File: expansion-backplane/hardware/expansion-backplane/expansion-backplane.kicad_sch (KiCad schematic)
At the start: 15 parts, among them J1 Barrel_Jack, SW1 SW_SPST

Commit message: added expansion connector
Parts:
- D1: footprint (none) -> LED_THT:LED_D3.0mm
- R1: footprint (none) -> Resistor_THT:R_Axial_DIN0207_L6.3mm_D2.5mm_P7.62mm_Horizontal
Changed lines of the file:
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@@
 			)
 		)
-		(property "Footprint" ""
+		(property "Footprint" "LED_THT:LED_D3.0mm"
 			(at 71.12 34.29 0)
 			(effects
@@
 			)
 		)
-		(property "Footprint" ""
+		(property "Footprint" "Resistor_THT:R_Axial_DIN0207_L6.3mm_D2.5mm_P7.62mm_Horizontal"
 			(at 69.342 44.45 90)
 			(effects

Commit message: wip
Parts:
- removed SW1: SW_SPST, symbol Switch:SW_SPST
- added SW1: SW_SPDT, minimal-64x4:E-Switch_200MSP1T2B2M6RE, symbol Switch:SW_SPDT
- C1: renamed from C2; footprint (none) -> Capacitor_THT:CP_Radial_D4.0mm_P2.00mm
- C2: renamed from C1; footprint (none) -> Capacitor_THT:CP_Radial_D5.0mm_P2.00mm
- C3, C4, C5, C6: footprint (none) -> Capacitor_THT:CP_Radial_D4.0mm_P2.00mm
- CN1, CN2, CN3, CN4, CN5: footprint Connector_PinSocket_2.54mm:PinSocket_2x32_P2.54mm_Vertical -> Connector_PinSocket_2.54mm:PinSocket_2x16_P2.54mm_Vertical
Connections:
- net +5V: now also SW1.1 (A)
- net at J1.1: now also SW1.2 (B)
- no-connect marks 0 -> 1
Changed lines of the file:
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@@
 	)
 	(junction
-		(at 71.12 30.48)
+		(at 170.18 95.25)
 		(diameter 0)
 		(color 0 0 0 0)
 	)
 	(junction
-		(at 170.18 95.25)
+		(at 215.9 95.25)
 		(diameter 0)
 		(color 0 0 0 0)
 	)
 	(junction
-		(at 215.9 95.25)
+		(at 71.12 30.48)
 		(diameter 0)
 		(color 0 0 0 0)
 	)
+	(no_connect
+		(at 67.31 33.02)
+	)
 	(wire
 		(pts
@@
 	(wire
 		(pts
+			(xy 71.12 27.94) (xy 71.12 30.48)
+		)
+		(stroke
+			(width 0)
+			(type default)
+		)
+	)
+	(wire
+		(pts
 			(xy 81.28 48.26) (xy 81.28 38.1)
 		)
@@
 	(wire
 		(pts
+			(xy 67.31 27.94) (xy 71.12 27.94)
+		)
+		(stroke
+			(width 0)
+			(type default)
+		)
+	)
+	(wire
+		(pts
 			(xy 38.1 95.25) (xy 40.64 95.25)
 		)
@@
 	(wire
 		(pts
-			(xy 67.31 30.48) (xy 71.12 30.48)
-		)
-		(stroke
-			(width 0)
-			(type default)
-		)
-	)
-	(wire
-		(pts
 			(xy 83.82 95.25) (xy 83.82 85.09)
 		)
@@
 		(on_board yes)
 		(dnp no)
-		(property "Reference" "C2"
+		(property "Reference" "C1"
 			(at 50.8 79.248 90)
 			(effects
@@
 			)
 		)
-		(property "Footprint" ""
+		(property "Footprint" "Capacitor_THT:CP_Radial_D4.0mm_P2.00mm"
 			(at 54.61 84.1248 0)
 			(effects
@@
 			(project "expansion-backplane"
 				(path "/e49372f6-369a-421a-b977-37c09b53354c"
-					(reference "C2")
+					(reference "C1")
 					(unit 1)
 				)
@@
 		(dnp no)
 		(fields_autoplaced yes)
-		(property "Reference" "#PWR02"
+		(property "Reference" "#PWR01"
 			(at 38.1 99.06 0)
 			(effects
@@
 			(project "expansion-backplane"
 				(path "/e49372f6-369a-421a-b977-37c09b53354c"
-					(reference "#PWR02")
+					(reference "#PWR01")
 					(unit 1)
 				)
@@
 			)
 		)
-		(property "Footprint" "Connector_PinSocket_2.54mm:PinSocket_2x32_P2.54mm_Vertical"
+		(property "Footprint" "Connector_PinSocket_2.54mm:PinSocket_2x16_P2.54mm_Vertical"
 			(at 129.794 34.29 0)
 			(effects
@@
 		(dnp no)
 		(fields_autoplaced yes)
-		(property "Reference" "#PWR010"
+		(property "Reference" "#PWR012"
 			(at 238.76 88.9 0)
 			(effects
@@
 			(project "expansion-backplane"
 				(path "/e49372f6-369a-421a-b977-37c09b53354c"
-					(reference "#PWR010")
+					(reference "#PWR012")
 					(unit 1)
 				)
@@
 		(dnp no)
 		(fields_autoplaced yes)
-		(property "Reference" "C1"
+		(property "Reference" "C2"
 			(at 84.201 32.1888 0)
 			(effects
@@
 			)
 		)
-		(property "Footprint" ""
+		(property "Footprint" "Capacitor_THT:CP_Radial_D5.0mm_P2.00mm"
 			(at 82.2452 38.1 0)
 			(effects
@@
 			(project "expansion-backplane"
 				(path "/e49372f6-369a-421a-b977-37c09b53354c"
-					(reference "C1")
+					(reference "C2")
 					(unit 1)
 				)
@@
 		(dnp no)
 		(fields_autoplaced yes)
-		(property "Reference" "#PWR09"
+		(property "Reference" "#PWR011"
 			(at 213.36 99.06 0)
 			(effects
@@
 			(project "expansion-backplane"
 				(path "/e49372f6-369a-421a-b977-37c09b53354c"
-					(reference "#PWR09")
+					(reference "#PWR011")
 					(unit 1)
 				)
@@
 	)
 	(symbol
+		(lib_id "Switch:SW_SPDT")
+		(at 62.23 30.48 0)
+		(unit 1)
+		(exclude_from_sim no)
+		(in_bom yes)
+		(on_board yes)
+		(dnp no)
+		(fields_autoplaced yes)
+		(property "Reference" "SW1"
+			(at 62.23 22.6525 0)
+			(effects
+				(font
+					(size 1.27 1.27)
+				)
+			)
+		)
+		(property "Value" "SW_SPDT"
+			(at 62.23 25.0768 0)
+			(effects
+				(font
+					(size 1.27 1.27)
+				)
+			)
+		)
+		(property "Footprint" "minimal-64x4:E-Switch_200MSP1T2B2M6RE"
+			(at 62.23 30.48 0)
+			(effects
+				(font
+					(size 1.27 1.27)
+				)
+				(hide yes)
+			)
+		)
+		(property "Datasheet" "https://configured-product-images.s3.amazonaws.com/2D/specs/200MSP1T2B2M6RE.pdf"
+			(at 62.23 38.1 0)
+			(effects
+				(font
+					(size 1.27 1.27)
+				)
+				(hide yes)
+			)
+		)
+		(property "Description" "Switch, single pole double throw"
+			(at 62.23 30.48 0)
+			(effects
+				(font
+					(size 1.27 1.27)
+				)
+				(hide yes)
+			)
+		)
+		(pin "2"
+		)
+		(pin "1"
+		)
+		(pin "3"
+		)
+		(instances
+			(project "expansion-backplane"
+				(path "/e49372f6-369a-421a-b977-37c09b53354c"
+					(reference "SW1")
+					(unit 1)
+				)
+			)
+		)
+	)
+	(symbol
 		(lib_name "min-64x4-expansion_1")
 		(lib_id "minimal-64x4:min-64x4-expansion")
@@
 			)
 		)
-		(property "Footprint" "Connector_PinSocket_2.54mm:PinSocket_2x32_P2.54mm_Vertical"
+		(property "Footprint" "Connector_PinSocket_2.54mm:PinSocket_2x16_P2.54mm_Vertical"
 			(at 261.874 34.29 0)
 			(effects
@@
 			)
 		)
-		(property "Footprint" ""
+		(property "Footprint" "Capacitor_THT:CP_Radial_D4.0mm_P2.00mm"
 			(at 184.15 84.1248 0)
 			(effects
@@
 		(dnp no)
 		(fields_autoplaced yes)
-		(property "Reference" "#PWR05"
+		(property "Reference" "#PWR07"
 			(at 124.46 99.06 0)
 			(effects
@@
 			(project "expansion-backplane"
 				(path "/e49372f6-369a-421a-b977-37c09b53354c"
-					(reference "#PWR05")
+					(reference "#PWR07")
 					(unit 1)
 				)
@@
 		(dnp no)
 		(fields_autoplaced yes)
-		(property "Reference" "#PWR011"
+		(property "Reference" "#PWR05"
 			(at 90.17 54.61 0)
 			(effects
@@
 			(project "expansion-backplane"
 				(path "/e49372f6-369a-421a-b977-37c09b53354c"
-					(reference "#PWR011")
+					(reference "#PWR05")
 					(unit 1)
 				)
@@
 			)
 		)
-		(property "Footprint" "Connector_PinSocket_2.54mm:PinSocket_2x32_P2.54mm_Vertical"
+		(property "Footprint" "Connector_PinSocket_2.54mm:PinSocket_2x16_P2.54mm_Vertical"
 			(at 86.614 34.29 0)
 			(effects
@@
 			)
 		)
-		(property "Footprint" ""
+		(property "Footprint" "Capacitor_THT:CP_Radial_D4.0mm_P2.00mm"
 			(at 97.79 84.1248 0)
 			(effects
@@
 		(dnp no)
 		(fields_autoplaced yes)
-		(property "Reference" "#PWR07"
+		(property "Reference" "#PWR09"
 			(at 167.64 99.06 0)
 			(effects
@@
 			(project "expansion-backplane"
 				(path "/e49372f6-369a-421a-b977-37c09b53354c"
-					(reference "#PWR07")
+					(reference "#PWR09")
 					(unit 1)
 				)
@@
 			)
 		)
-		(property "Footprint" ""
+		(property "Footprint" "Capacitor_THT:CP_Radial_D4.0mm_P2.00mm"
 			(at 229.87 84.1248 0)
 			(effects
@@
 	)
 	(symbol
-		(lib_id "Switch:SW_SPST")
-		(at 62.23 30.48 0)
-		(unit 1)
-		(exclude_from_sim no)
-		(in_bom yes)
-		(on_board yes)
-		(dnp no)
-		(fields_autoplaced yes)
-		(property "Reference" "SW1"
-			(at 62.23 24.6845 0)
-			(effects
-				(font
-					(size 1.27 1.27)
-				)
-			)
-		)
-		(property "Value" "SW_SPST"
-			(at 62.23 27.1088 0)
-			(effects
-				(font
-					(size 1.27 1.27)
-				)
-			)
-		)
-		(property "Footprint" ""
-			(at 62.23 30.48 0)
-			(effects
-				(font
-					(size 1.27 1.27)
-				)
-				(hide yes)
-			)
-		)
-		(property "Datasheet" "~"
-			(at 62.23 30.48 0)
-			(effects
-				(font
-					(size 1.27 1.27)
-				)
-				(hide yes)
-			)
-		)
-		(property "Description" "Single Pole Single Throw (SPST) switch"
-			(at 62.23 30.48 0)
-			(effects
-				(font
-					(size 1.27 1.27)
-				)
-				(hide yes)
-			)
-		)
-		(pin "1"
-		)
-		(pin "2"
-		)
-		(instances
-			(project "expansion-backplane"
-				(path "/e49372f6-369a-421a-b977-37c09b53354c"
-					(reference "SW1")
-					(unit 1)
-				)
-			)
-		)
-	)
-	(symbol
 		(lib_id "power:GND")
 		(at 63.5 95.25 180)
@@
 		(dnp no)
 		(fields_autoplaced yes)
-		(property "Reference" "#PWR01"
+		(property "Reference" "#PWR02"
 			(at 63.5 88.9 0)
 			(effects
@@
 			(project "expansion-backplane"
 				(path "/e49372f6-369a-421a-b977-37c09b53354c"
-					(reference "#PWR01")
+					(reference "#PWR02")
 					(unit 1)
 				)
@@
 		(dnp no)
 		(fields_autoplaced yes)
-		(property "Reference" "#PWR06"
+		(property "Reference" "#PWR08"
 			(at 149.86 88.9 0)
 			(effects
@@
 			(project "expansion-backplane"
 				(path "/e49372f6-369a-421a-b977-37c09b53354c"
-					(reference "#PWR06")
+					(reference "#PWR08")
 					(unit 1)
 				)
@@
 		(dnp no)
 		(fields_autoplaced yes)
-		(property "Reference" "#PWR08"
+		(property "Reference" "#PWR010"
 			(at 193.04 88.9 0)
 			(effects
@@
 			(project "expansion-backplane"
 				(path "/e49372f6-369a-421a-b977-37c09b53354c"
-					(reference "#PWR08")
+					(reference "#PWR010")
 					(unit 1)
 				)
@@
 		(dnp no)
 		(fields_autoplaced yes)
-		(property "Reference" "#PWR04"
+		(property "Reference" "#PWR06"
 			(at 106.68 88.9 0)
 			(effects
@@
 			(project "expansion-backplane"
 				(path "/e49372f6-369a-421a-b977-37c09b53354c"
-					(reference "#PWR04")
+					(reference "#PWR06")
 					(unit 1)
 				)
@@
 			)
 		)
-		(property "Footprint" "Connector_PinSocket_2.54mm:PinSocket_2x32_P2.54mm_Vertical"
+		(property "Footprint" "Connector_PinSocket_2.54mm:PinSocket_2x16_P2.54mm_Vertical"
 			(at 172.974 34.29 0)
 			(effects
@@
 		(dnp no)
 		(fields_autoplaced yes)
-		(property "Reference" "#PWR012"
+		(property "Reference" "#PWR04"
 			(at 90.17 34.29 0)
 			(effects
@@
 			(project "expansion-backplane"
 				(path "/e49372f6-369a-421a-b977-37c09b53354c"
-					(reference "#PWR012")
+					(reference "#PWR04")
 					(unit 1)
 				)
@@
 			)
 		)
-		(property "Footprint" ""
+		(property "Footprint" "Capacitor_THT:CP_Radial_D4.0mm_P2.00mm"
 			(at 140.97 84.1248 0)
 			(effects
@@
 			)
 		)
-		(property "Footprint" "Connector_PinSocket_2.54mm:PinSocket_2x32_P2.54mm_Vertical"
+		(property "Footprint" "Connector_PinSocket_2.54mm:PinSocket_2x16_P2.54mm_Vertical"
 			(at 216.154 34.29 0)
 			(effects

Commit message: improved backplane
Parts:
- added C4: 0.1 uF, Capacitor_THT:C_Disc_D3.8mm_W2.6mm_P2.50mm, symbol Device:C
- added U1: 74LS126, Package_DIP:DIP-14_W7.62mm, symbol 74xx:74LS126
- renumbered C4 to C5, C5 to C6, C6 to C7
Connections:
- net +5V: now also C4.1, U1.12, U1.14 (VCC), U1.2, U1.5, U1.9
- net GND: now also C4.2, U1.7 (GND)
- net USER: no longer CN5.4 (NC)
- removed net INH: CN1.3 (INH), CN2.3 (INH), CN3.3 (INH), CN4.3 (INH), CN5.3 (INH)
- new net: CN2.3 (INH), U1.4
- new net: CN5.3 (INH), U1.11, U1.3, U1.6, U1.8
- new net: CN4.3 (INH), U1.13
- new net: CN3.3 (INH), U1.10
- new net: CN1.3 (INH), U1.1

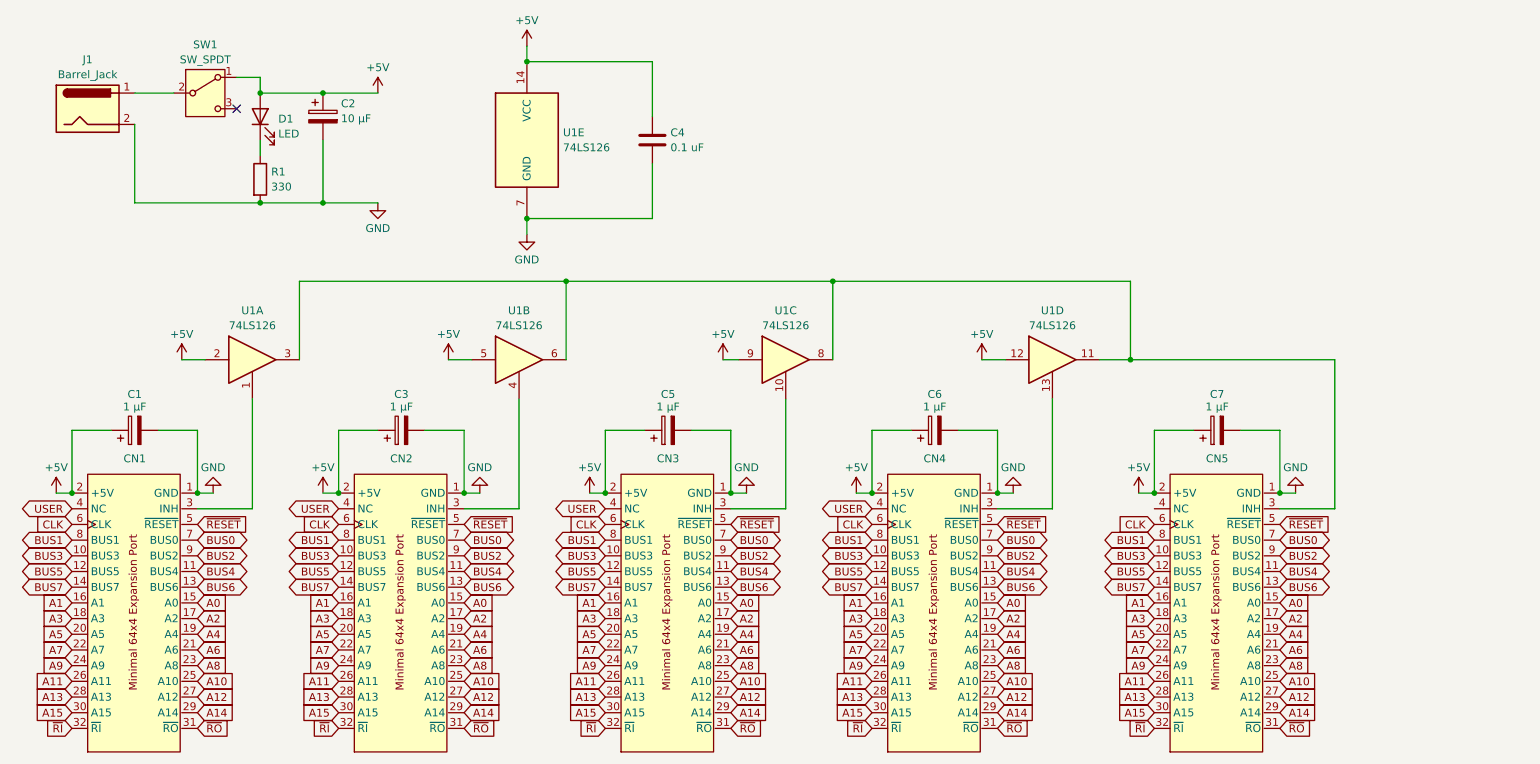
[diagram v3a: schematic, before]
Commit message: added pull down resistors
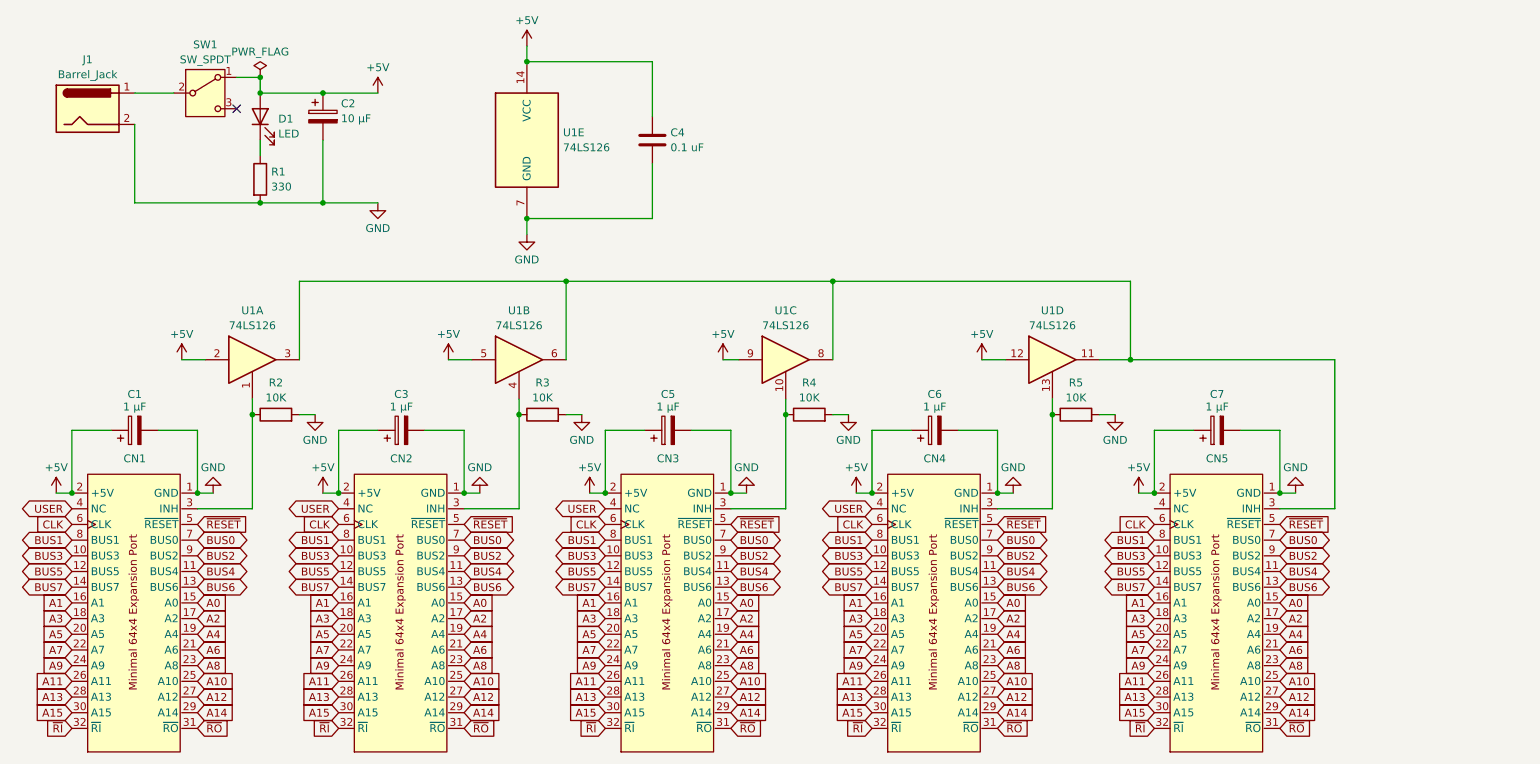
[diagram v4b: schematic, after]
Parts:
- added R2, R3, R4, R5: 10K, Resistor_THT:R_Axial_DIN0207_L6.3mm_D2.5mm_P7.62mm_Horizontal, symbol Device:R
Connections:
- net GND: now also R2.2, R3.2, R4.2, R5.2
- net at CN2.3 (INH), U1.4: now also R3.1
- net at CN4.3 (INH), U1.13: now also R5.1
- net at CN3.3 (INH), U1.10: now also R4.1
- net at CN1.3 (INH), U1.1: now also R2.1

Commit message: added pull down resistor
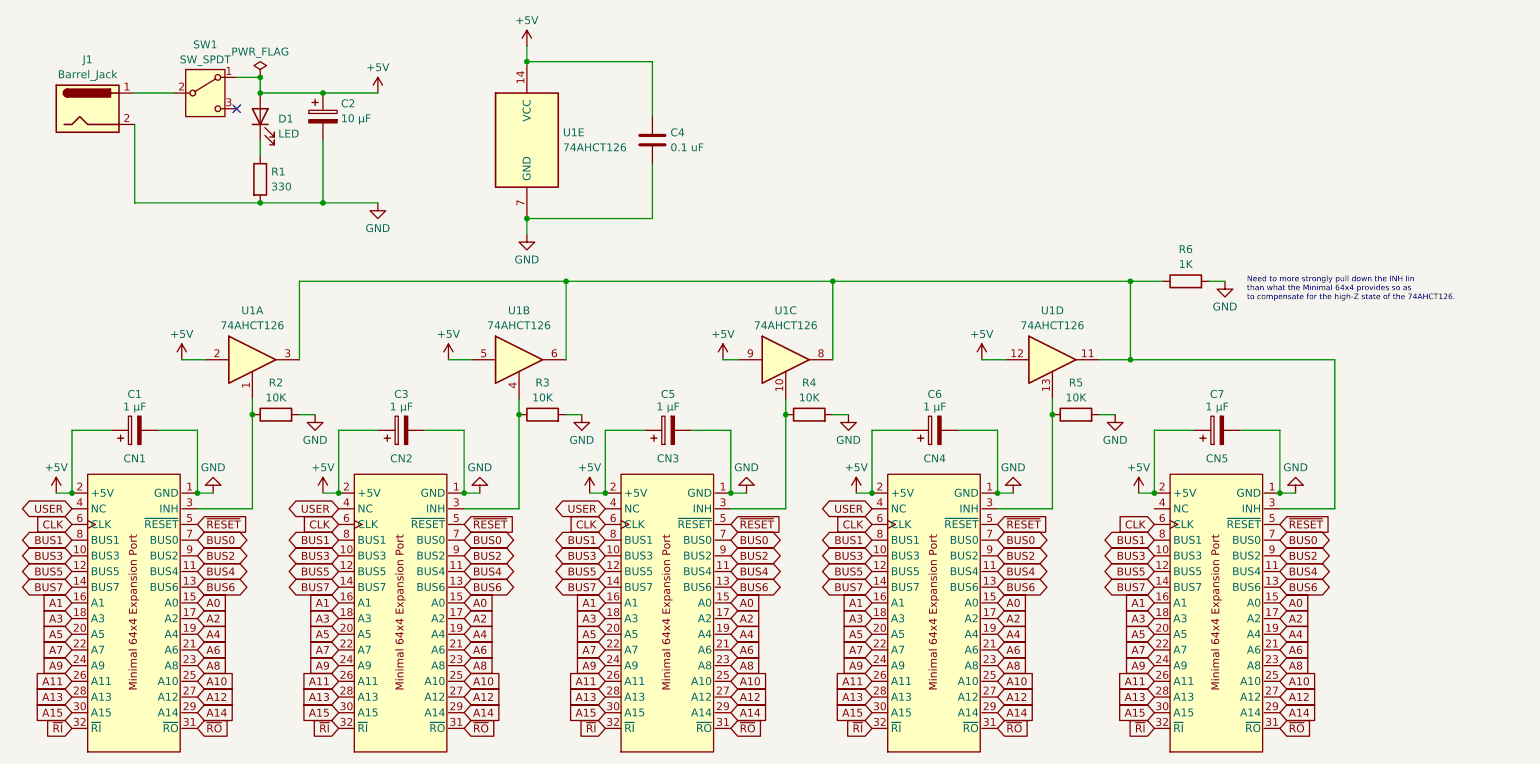
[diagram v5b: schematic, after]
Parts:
- added R6: 1K, Resistor_THT:R_Axial_DIN0207_L6.3mm_D2.5mm_P7.62mm_Horizontal, symbol Device:R
- U1: value 74LS126 -> 74AHCT126
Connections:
- net GND: now also R6.2
- net at CN5.3 (INH), U1.11, U1.3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: now also R6.1
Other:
- note added: "Need to more strongly pull down the INH lin than what the Minimal 64x4 provides so as to compensate for the high-Z state of the 74AHCT126."
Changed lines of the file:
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@@
 	)
 	(junction
+		(at 212.0242 60.96)
+		(diameter 0)
+		(color 0 0 0 0)
+	)
+	(junction
 		(at 236.22 95.25)
 		(diameter 0)
@@
 	(wire
 		(pts
-			(xy 245.11 97.79) (xy 245.11 73.66)
+			(xy 245.11 73.66) (xy 245.11 97.79)
 		)
 		(stroke
@@
 	(wire
 		(pts
+			(xy 212.0242 60.96) (xy 217.17 60.96)
+		)
+		(stroke
+			(width 0)
+			(type default)
+		)
+	)
+	(wire
+		(pts
 			(xy 127 95.25) (xy 127 85.09)
 		)
@@
 	(wire
 		(pts
+			(xy 224.79 60.96) (xy 227.33 60.96)
+		)
+		(stroke
+			(width 0)
+			(type default)
+		)
+	)
+	(wire
+		(pts
 			(xy 71.12 30.48) (xy 81.28 30.48)
 		)
@@
 		)
 	)
+	(text "Need to more strongly pull down the INH lin\nthan what the Minimal 64x4 provides so as\nto compensate for the high-Z state of the 74AHCT126."
+		(exclude_from_sim no)
+		(at 230.886 62.23 0)
+		(effects
+			(font
+				(size 0.9 0.9)
+			)
+			(justify left)
+		)
+	)
 	(global_label "~{RI}"
 		(shape input)
@@
 			)
 		)
-		(property "Value" "74LS126"
+		(property "Value" "74AHCT126"
 			(at 120.142 39.3121 0)
 			(effects
@@
 			)
 		)
-		(property "Value" "74LS126"
+		(property "Value" "74AHCT126"
 			(at 113.03 68.1298 0)
 			(effects
@@
 			)
 		)
-		(property "Value" "74LS126"
+		(property "Value" "74AHCT126"
 			(at 199.39 68.1298 0)
 			(effects
@@
 	)
 	(symbol
+		(lib_id "Device:R")
+		(at 220.98 60.96 90)
+		(unit 1)
+		(exclude_from_sim no)
+		(in_bom yes)
+		(on_board yes)
+		(dnp no)
+		(fields_autoplaced yes)
+		(property "Reference" "R6"
+			(at 220.98 55.7995 90)
+			(effects
+				(font
+					(size 1.27 1.27)
+				)
+			)
+		)
+		(property "Value" "1K"
+			(at 220.98 58.2238 90)
+			(effects
+				(font
+					(size 1.27 1.27)
+				)
+			)
+		)
+		(property "Footprint" "Resistor_THT:R_Axial_DIN0207_L6.3mm_D2.5mm_P7.62mm_Horizontal"
+			(at 220.98 62.738 90)
+			(effects
+				(font
+					(size 1.27 1.27)
+				)
+				(hide yes)
+			)
+		)
+		(property "Datasheet" "~"
+			(at 220.98 60.96 0)
+			(effects
+				(font
+					(size 1.27 1.27)
+				)
+				(hide yes)
+			)
+		)
+		(property "Description" "Resistor"
+			(at 220.98 60.96 0)
+			(effects
+				(font
+					(size 1.27 1.27)
+				)
+				(hide yes)
+			)
+		)
+		(pin "2"
+		)
+		(pin "1"
+		)
+		(instances
+			(project ""
+				(path "/e49372f6-369a-421a-b977-37c09b53354c"
+					(reference "R6")
+					(unit 1)
+				)
+			)
+		)
+	)
+	(symbol
 		(lib_id "power:GND")
 		(at 209.55 82.55 0)
@@
 	)
 	(symbol
+		(lib_id "power:GND")
+		(at 227.33 60.96 0)
+		(unit 1)
+		(exclude_from_sim no)
+		(in_bom yes)
+		(on_board yes)
+		(dnp no)
+		(fields_autoplaced yes)
+		(property "Reference" "#PWR023"
+			(at 227.33 67.31 0)
+			(effects
+				(font
+					(size 1.27 1.27)
+				)
+				(hide yes)
+			)
+		)
+		(property "Value" "GND"
+			(at 227.33 65.0931 0)
+			(effects
+				(font
+					(size 1.27 1.27)
+				)
+			)
+		)
+		(property "Footprint" ""
+			(at 227.33 60.96 0)
+			(effects
+				(font
+					(size 1.27 1.27)
+				)
+				(hide yes)
+			)
+		)
+		(property "Datasheet" ""
+			(at 227.33 60.96 0)
+			(effects
+				(font
+					(size 1.27 1.27)
+				)
+				(hide yes)
+			)
+		)
+		(property "Description" "Power symbol creates a global label with name \"GND\" , ground"
+			(at 227.33 60.96 0)
+			(effects
+				(font
+					(size 1.27 1.27)
+				)
+				(hide yes)
+			)
+		)
+		(pin "1"
+		)
+		(instances
+			(project ""
+				(path "/e49372f6-369a-421a-b977-37c09b53354c"
+					(reference "#PWR023")
+					(unit 1)
+				)
+			)
+		)
+	)
+	(symbol
 		(lib_id "74xx:74LS126")
 		(at 156.21 73.66 0)
@@
 			)
 		)
-		(property "Value" "74LS126"
+		(property "Value" "74AHCT126"
 			(at 156.21 68.1298 0)
 			(effects
@@
 			)
 		)
-		(property "Value" "74LS126"
+		(property "Value" "74AHCT126"
 			(at 69.85 68.1298 0)
 			(effects
